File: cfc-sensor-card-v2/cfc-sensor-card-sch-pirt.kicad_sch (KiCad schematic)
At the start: 75 parts, among them U1 TLC3704, U10 LT3042IMSE, U11 LT3042IMSE, U12 U-PIRT-PIRT1280A1-12, U13 XO_ISM95-XXXXXX, U6 LP2985-3.3, U7 LT3042IMSE, U8 LT3042IMSE, U9 LT3042IMSE

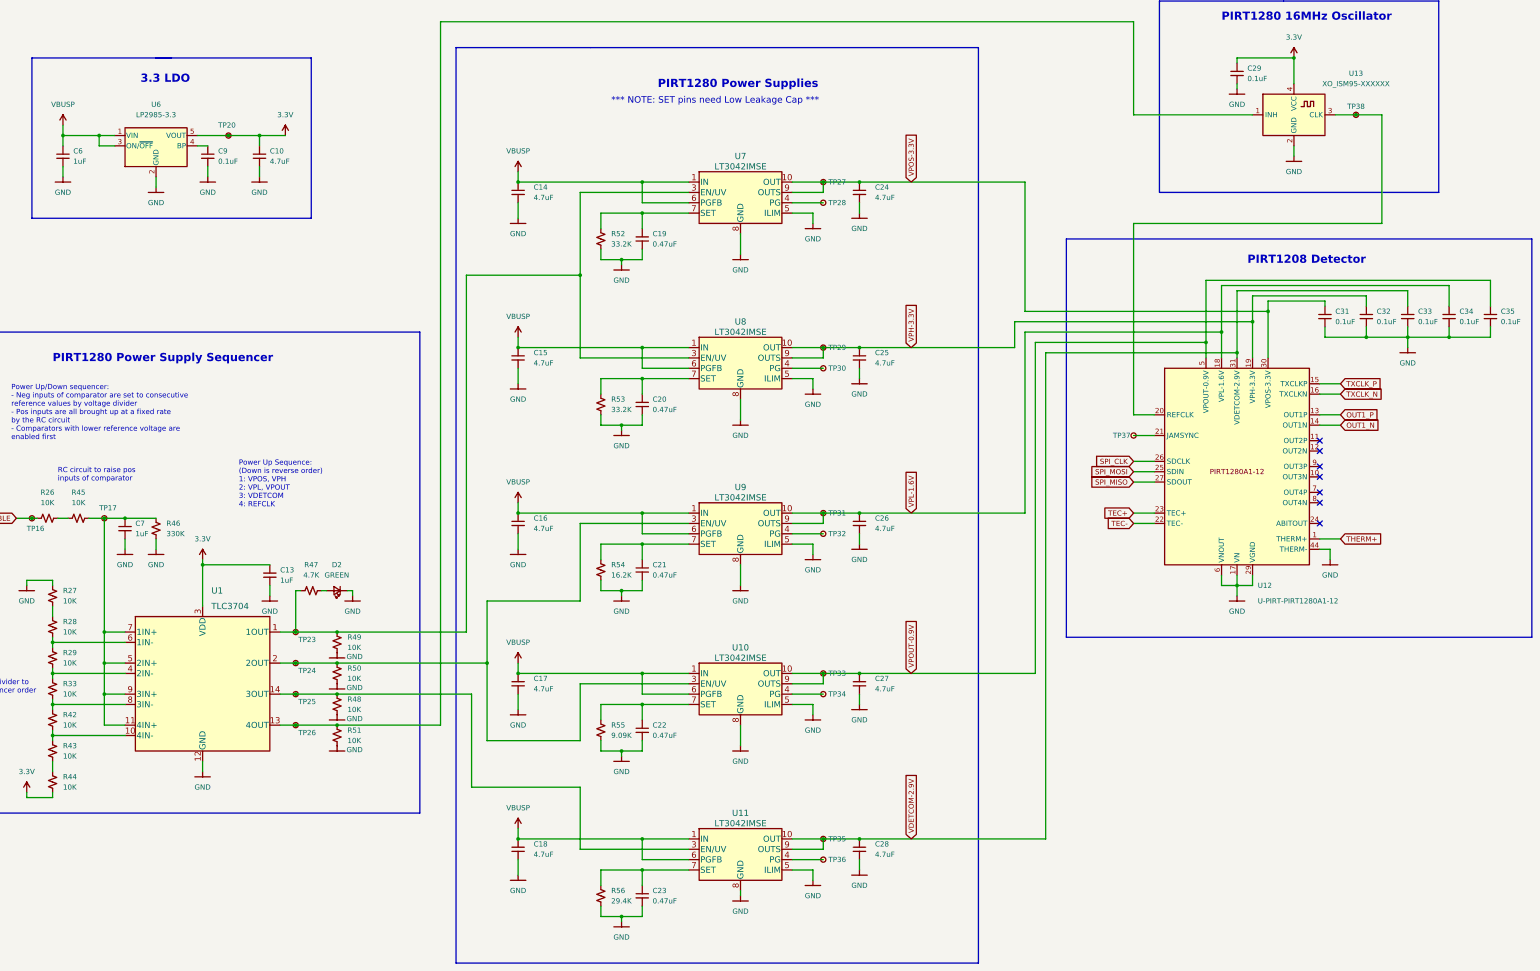
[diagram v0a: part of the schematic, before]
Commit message: Fix and complete BOM, fix lots of little layout issue and footprint inconsistancies, and polish. Ready to go!
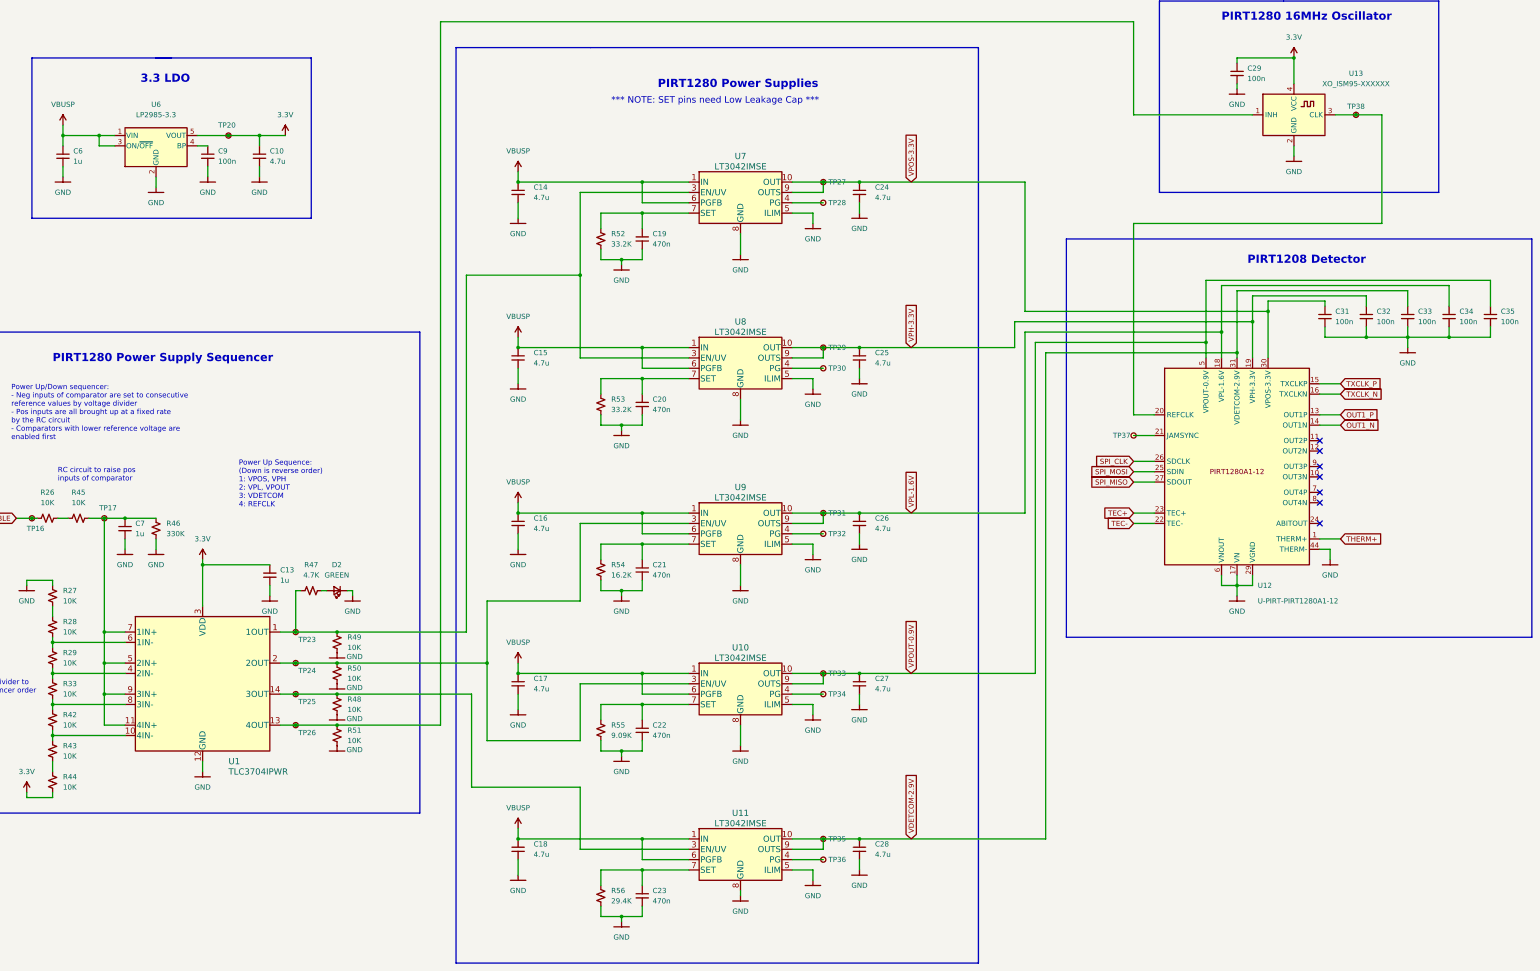
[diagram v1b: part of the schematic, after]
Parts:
- C10, C14, C15, C16, C17, C18, C24, C25, C26, C27, C28: value 4.7uF -> 4.7u; DIS (none) -> DigiKey; DPN (none) -> 587-4332-1-ND; MFR (none) -> Taiyo Yuden; MPN (none) -> EMK107BBJ475KAHT
- C13, C6, C7: value 1uF -> 1u; DIS (none) -> DigiKey; DPN (none) -> 587-3473-1-ND; MFR (none) -> Taiyo Yuden; MPN (none) -> TMK107BJ105KAHT
- C19, C20, C21, C22, C23: value 0.47uF -> 470n; DIS (none) -> DigiKey; DPN (none) -> 587-3476-1-ND; MFR (none) -> Taiyo Yuden; MPN (none) -> TMK107BJ474KAHT
- C29, C31, C32, C33, C34, C35, C9: value 0.1uF -> 100n; DIS (none) -> DigiKey; DPN (none) -> 587-3472-1-ND; MFR (none) -> Taiyo Yuden; MPN (none) -> TMK107BJ104KAHT
- D2: DIS (none) -> DigiKey; DPN (none) -> 732-4971-1-ND; MFR (none) -> Wurth; MPN (none) -> 150060GS75000
- R26, R27, R28, R29, R33, R42, R43, R44, R45, R48, R49, R50, R51: DIS (none) -> DigiKey; DPN (none) -> RMCF0603FT10K0CT-ND; MFR (none) -> Stackpole Electronics Inc; MPN (none) -> RMCF0603FT10K0
- R46: DIS (none) -> DigiKey; DPN (none) -> RMCF0603FT330KCT-ND; MFR (none) -> Stackpole Electronics Inc; MPN (none) -> RMCF0603FT330K
- R47: DIS (none) -> DigiKey; DPN (none) -> RMCF0603FT4K70CT-ND; MFR (none) -> Stackpole Electronics Inc; MPN (none) -> RMCF0603FT4K70
- R52, R53: DIS (none) -> DigiKey; DPN (none) -> RMCF0603FT33K2CT-ND; MFR (none) -> Stackpole Electronics Inc; MPN (none) -> RMCF0603FT33K2
- R54: DIS (none) -> DigiKey; DPN (none) -> RMCF0603FT16K2CT-ND; MFR (none) -> Stackpole Electronics Inc; MPN (none) -> RMCF0603FT16K2
- R55: DIS (none) -> DigiKey; DPN (none) -> RMCF0603FT9K09CT-ND; MFR (none) -> Stackpole Electronics Inc; MPN (none) -> RMCF0603FT9K09
- R56: DIS (none) -> DigiKey; DPN (none) -> 738-RMCF0603FT29K4CT-ND; MFR (none) -> Stackpole Electronics Inc; MPN (none) -> RMCF0603FT29K4
- TP16, TP17, TP20, TP23, TP24, TP25, TP26, TP27, TP28, TP29, TP30, TP31, TP32, TP33, TP34, TP35, TP36, TP37, TP38: footprint oresat-misc:TestPoint-0.75mm-th -> oresat-misc:TestPoint-MinTH; now left out of the parts list
- U1: value TLC3704 -> TLC3704IPWR; DIS (none) -> DigiKey; DPN (none) -> 296-39242-1-ND; MFR (none) -> Texas Instruments; MPN (none) -> TLC3704IPWR
- U10, U11, U13, U6, U7, U8, U9: DIS (none) -> DigiKey; DIST Digikey -> (none)
- U12: DIS (none) -> N/A; DPN (none) -> N/A; MFR (none) -> Princeton IR; MPN (none) -> PIRT1280A1-12
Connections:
- now unconnected: U12.2, U12.28, U12.3, U12.32, U12.33, U12.34, U12.35, U12.36, U12.37, U12.38, U12.39, U12.4, U12.40, U12.41, U12.42, U12.43
